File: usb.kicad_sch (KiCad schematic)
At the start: 22 parts, among them Q1 MMBT3904-C20526, Q2 MMBT3904-C20526, SW2 SW_Push, U1 CP2102N-A02-GQFN24R

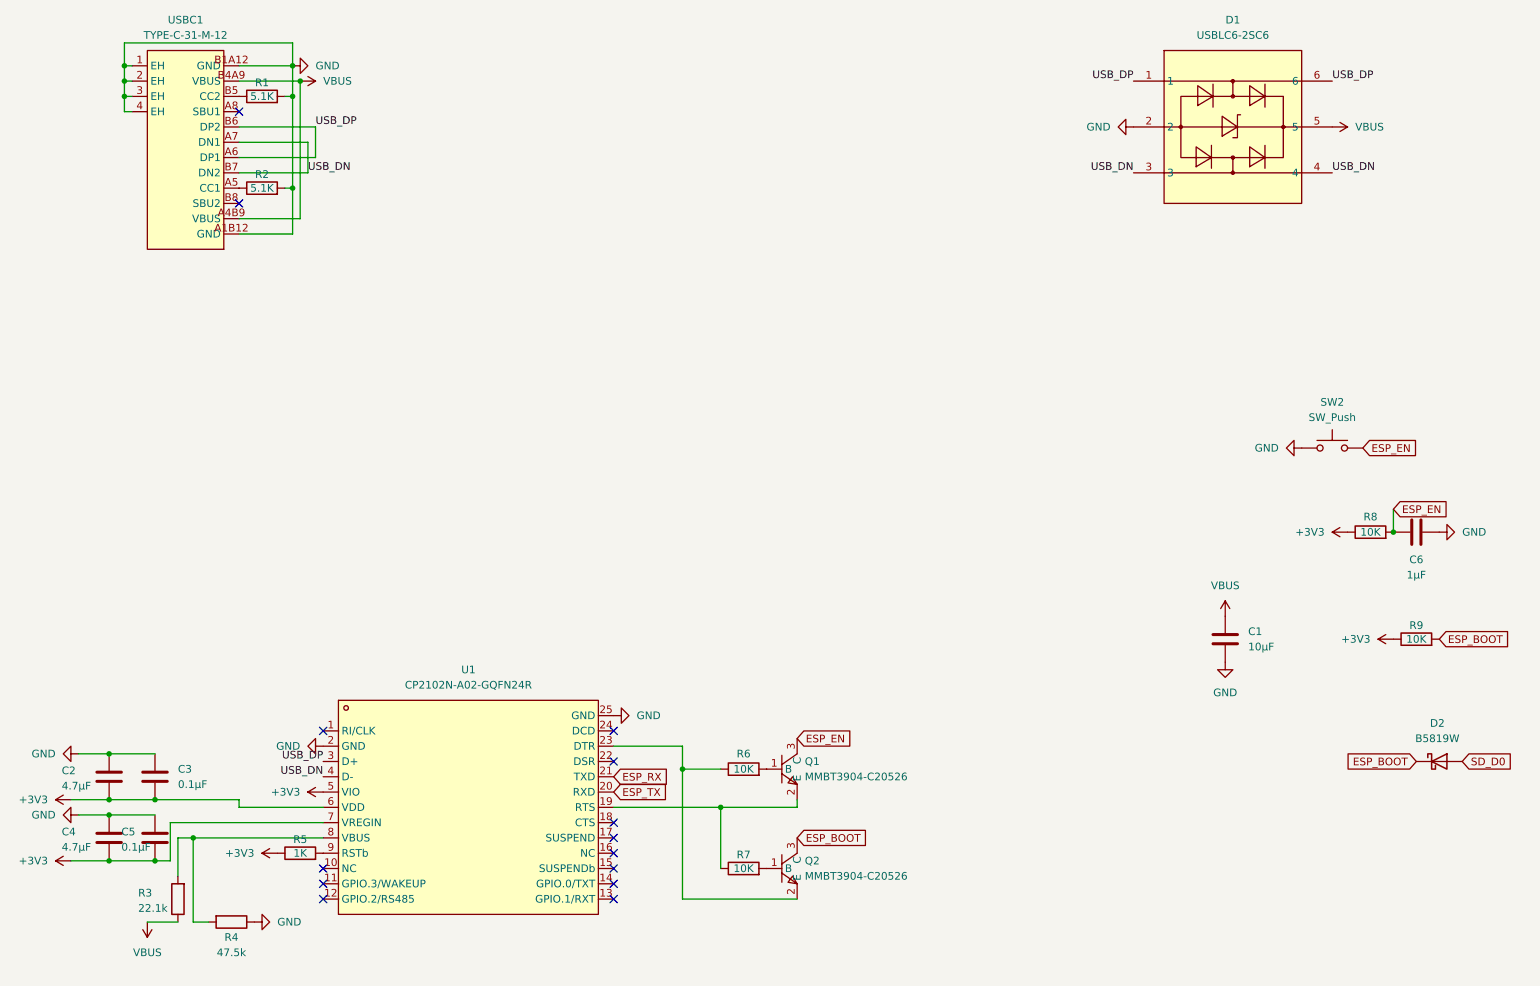
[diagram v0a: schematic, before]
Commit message: Schematic done
- sheet files renamed to English (usb, power, esp32, audio, io)
- final layout, annotation R1-R42 / C1-C43 / U1-U9 / J1-J4 / SW1-SW8
- all buttons are TS-1088, project R/C symbols, PWR_FLAGs
- connections.md replaces conexiuni.md (English, final references)
- final check on the KiCad netlist: 278/278 checks against connections.md
- status updated; firmware note: BQ25180 charge current defaults to ~10 mA

Co-Authored-By: Claude Opus 5.5 <noreply@anthropic.com>
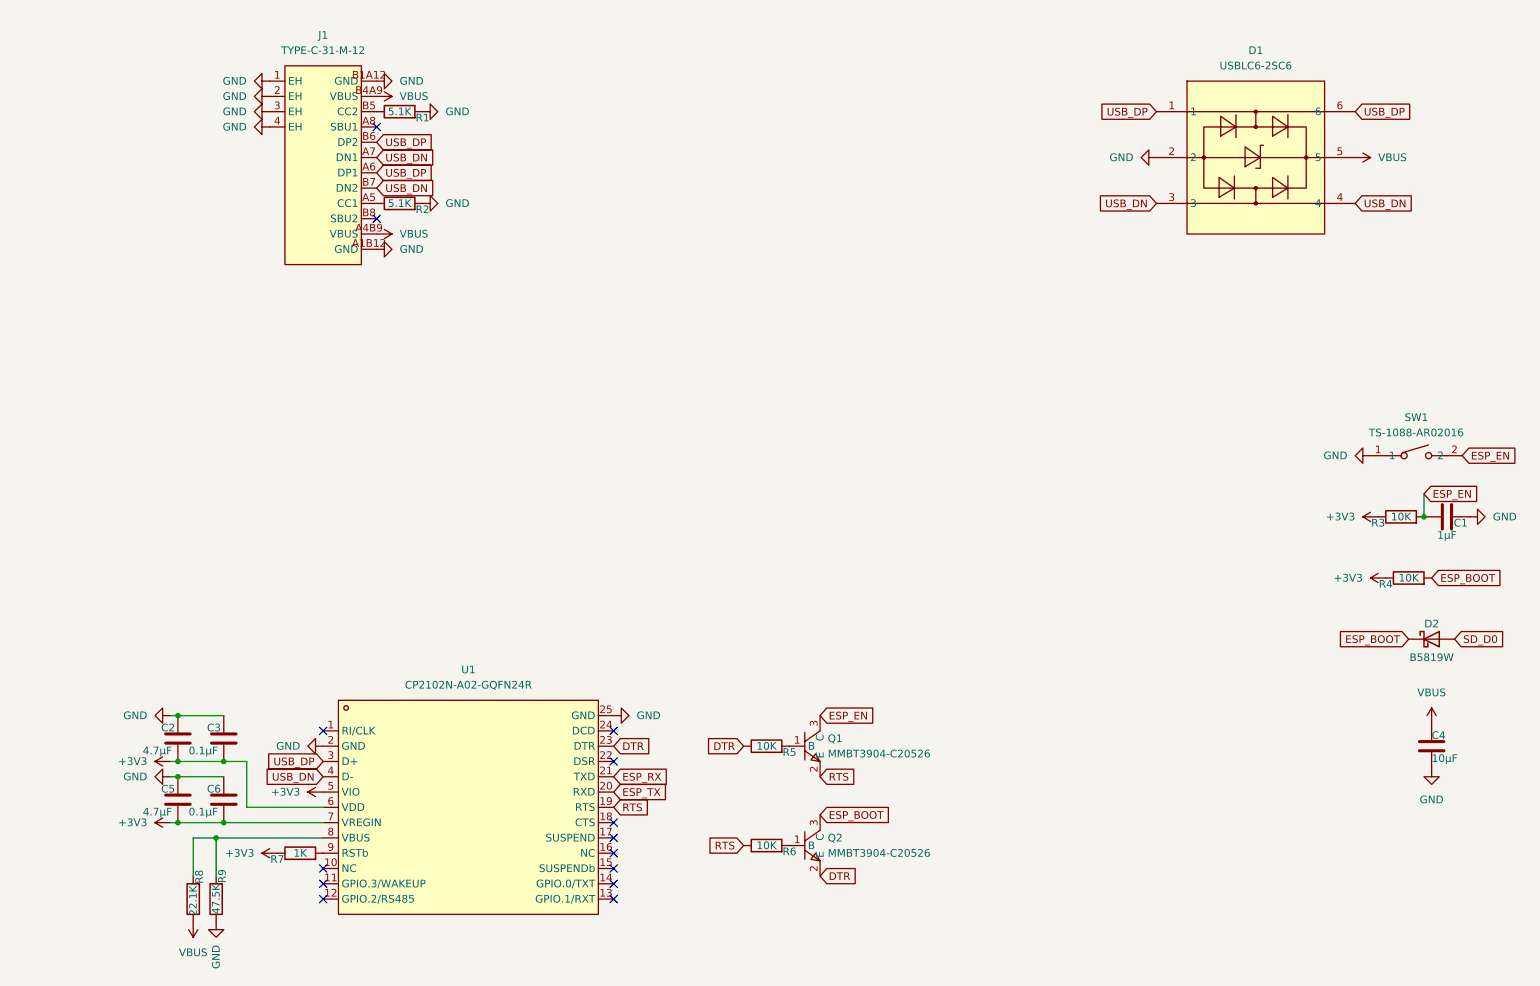
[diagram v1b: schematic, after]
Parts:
- removed SW2: SW_Push, symbol Switch:SW_Push
- added SW1: TS-1088-AR02016, mp3_player:SW-SMD_L3.9-W3.0-P4.45, symbol mp3_player:TS-1088-AR02016
- R1, R2: symbol Device:R -> mp3_player:R
- R3: renamed from R8; symbol Device:R -> mp3_player:R
- R4: renamed from R9; symbol Device:R -> mp3_player:R
- R5: renamed from R6; symbol Device:R -> mp3_player:R
- R6: renamed from R7; symbol Device:R -> mp3_player:R
- R7: renamed from R5; symbol Device:R -> mp3_player:R
- R8: renamed from R3; value 22.1k -> 22.1K; symbol Device:R -> mp3_player:R
- R9: renamed from R4; value 47.5k -> 47.5K; symbol Device:R -> mp3_player:R
- renumbered C6 to C1, C1 to C4, C4 to C5, C5 to C6, USBC1 to J1
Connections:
- net ESP_EN: now also SW1.2
- net GND: now also SW1.1
- net RTS: now reaches Q1.2 (E), R6.1, U1.19 (RTS)
- net DTR: now reaches Q2.2 (E), R5.1, U1.23 (DTR)
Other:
- moved on the sheet: C1, C2, C3, C4, C5, C6, D1, D2, J1, Q1, Q2, R1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

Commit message: Assign footprints and LCSC parts to passives, D2 and BT1
Thin-film 0.1% resistors in the audio path and rail dividers, C0G caps
in the DAC output filter, Samsung/Murata MLCCs with 0603/0805 cases for
bulk caps. Passive choices documented in mp3_player.md.

Co-Authored-By: Claude Opus 5.5 <noreply@anthropic.com>
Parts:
- C1: footprint (none) -> Capacitor_SMD:C_0402_1005Metric; LCSC Part (none) -> C52923
- C2, C5: footprint (none) -> Capacitor_SMD:C_0603_1608Metric; LCSC Part (none) -> C19666
- C3, C6: footprint (none) -> Capacitor_SMD:C_0402_1005Metric; LCSC Part (none) -> C1525
- C4: footprint (none) -> Capacitor_SMD:C_0805_2012Metric; LCSC Part (none) -> C15850
- D2: footprint (none) -> Diode_SMD:D_SOD-123; LCSC Part (none) -> C8598
- R1, R2: footprint (none) -> Resistor_SMD:R_0402_1005Metric; LCSC Part (none) -> C25905
- R3, R4, R5, R6: footprint (none) -> Resistor_SMD:R_0402_1005Metric; LCSC Part (none) -> C190095
- R7: footprint (none) -> Resistor_SMD:R_0402_1005Metric; LCSC Part (none) -> C11702
- R8: footprint (none) -> Resistor_SMD:R_0402_1005Metric; LCSC Part (none) -> C163478
- R9: footprint (none) -> Resistor_SMD:R_0402_1005Metric; LCSC Part (none) -> C137974
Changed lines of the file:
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@@
 			)
 		)
-		(property "Footprint" ""
+		(property "Footprint" "Resistor_SMD:R_0402_1005Metric"
+			(at 48.768 173.99 90)
+			(hide yes)
+			(show_name no)
+			(do_not_autoplace no)
+			(effects
+				(font
+					(size 1.27 1.27)
+				)
+			)
+		)
+				(property "LCSC Part" "C137974"
 			(at 48.768 173.99 90)
 			(hide yes)
@@
 			)
 		)
-		(property "Footprint" ""
+		(property "Footprint" "Resistor_SMD:R_0402_1005Metric"
+			(at 243.84 112.268 90)
+			(hide yes)
+			(show_name no)
+			(do_not_autoplace no)
+			(effects
+				(font
+					(size 1.27 1.27)
+				)
+			)
+		)
+				(property "LCSC Part" "C190095"
 			(at 243.84 112.268 90)
 			(hide yes)
@@
 			)
 		)
-		(property "Footprint" ""
+		(property "Footprint" "Resistor_SMD:R_0402_1005Metric"
+			(at 60.96 168.148 90)
+			(hide yes)
+			(show_name no)
+			(do_not_autoplace no)
+			(effects
+				(font
+					(size 1.27 1.27)
+				)
+			)
+		)
+				(property "LCSC Part" "C11702"
 			(at 60.96 168.148 90)
 			(hide yes)
@@
 			)
 		)
-		(property "Footprint" ""
+		(property "Footprint" "Capacitor_SMD:C_0603_1608Metric"
+			(at 39.6748 143.51 0)
+			(hide yes)
+			(show_name no)
+			(do_not_autoplace no)
+			(effects
+				(font
+					(size 1.27 1.27)
+				)
+			)
+		)
+				(property "LCSC Part" "C19666"
 			(at 39.6748 143.51 0)
 			(hide yes)
@@
 			)
 		)
-		(property "Footprint" ""
+		(property "Footprint" "Resistor_SMD:R_0402_1005Metric"
+			(at 44.958 173.99 90)
+			(hide yes)
+			(show_name no)
+			(do_not_autoplace no)
+			(effects
+				(font
+					(size 1.27 1.27)
+				)
+			)
+		)
+				(property "LCSC Part" "C163478"
 			(at 44.958 173.99 90)
 			(hide yes)
@@
 			)
 		)
-		(property "Footprint" ""
+		(property "Footprint" "Resistor_SMD:R_0402_1005Metric"
+			(at 245.11 122.428 90)
+			(hide yes)
+			(show_name no)
+			(do_not_autoplace no)
+			(effects
+				(font
+					(size 1.27 1.27)
+				)
+			)
+		)
+				(property "LCSC Part" "C190095"
 			(at 245.11 122.428 90)
 			(hide yes)
@@
 			)
 		)
-		(property "Footprint" ""
+		(property "Footprint" "Resistor_SMD:R_0402_1005Metric"
+			(at 138.43 166.878 90)
+			(hide yes)
+			(show_name no)
+			(do_not_autoplace no)
+			(effects
+				(font
+					(size 1.27 1.27)
+				)
+			)
+		)
+				(property "LCSC Part" "C190095"
 			(at 138.43 166.878 90)
 			(hide yes)
@@
 			)
 		)
-		(property "Footprint" ""
+		(property "Footprint" "Resistor_SMD:R_0402_1005Metric"
+			(at 138.43 150.368 90)
+			(hide yes)
+			(show_name no)
+			(do_not_autoplace no)
+			(effects
+				(font
+					(size 1.27 1.27)
+				)
+			)
+		)
+				(property "LCSC Part" "C190095"
 			(at 138.43 150.368 90)
 			(hide yes)
@@
 			)
 		)
-		(property "Footprint" ""
+		(property "Footprint" "Capacitor_SMD:C_0603_1608Metric"
+			(at 39.6748 153.67 0)
+			(hide yes)
+			(show_name no)
+			(do_not_autoplace no)
+			(effects
+				(font
+					(size 1.27 1.27)
+				)
+			)
+		)
+				(property "LCSC Part" "C19666"
 			(at 39.6748 153.67 0)
 			(hide yes)
@@
 			)
 		)
-		(property "Footprint" ""
+		(property "Footprint" "Capacitor_SMD:C_0402_1005Metric"
+			(at 47.2948 153.67 0)
+			(hide yes)
+			(show_name no)
+			(do_not_autoplace no)
+			(effects
+				(font
+					(size 1.27 1.27)
+				)
+			)
+		)
+				(property "LCSC Part" "C1525"
 			(at 47.2948 153.67 0)
 			(hide yes)
@@
 			)
 		)
-		(property "Footprint" ""
+		(property "Footprint" "Capacitor_SMD:C_0805_2012Metric"
+			(at 249.8852 152.4 0)
+			(hide yes)
+			(show_name no)
+			(do_not_autoplace no)
+			(effects
+				(font
+					(size 1.27 1.27)
+				)
+			)
+		)
+				(property "LCSC Part" "C15850"
 			(at 249.8852 152.4 0)
 			(hide yes)
@@
 			)
 		)
-		(property "Footprint" ""
+		(property "Footprint" "Capacitor_SMD:C_0402_1005Metric"
+			(at 247.65 111.4552 0)
+			(hide yes)
+			(show_name no)
+			(do_not_autoplace no)
+			(effects
+				(font
+					(size 1.27 1.27)
+				)
+			)
+		)
+				(property "LCSC Part" "C52923"
 			(at 247.65 111.4552 0)
 			(hide yes)
@@
 			)
 		)
-		(property "Footprint" ""
+		(property "Footprint" "Capacitor_SMD:C_0402_1005Metric"
+			(at 47.2948 143.51 0)
+			(hide yes)
+			(show_name no)
+			(do_not_autoplace no)
+			(effects
+				(font
+					(size 1.27 1.27)
+				)
+			)
+		)
+				(property "LCSC Part" "C1525"
 			(at 47.2948 143.51 0)
 			(hide yes)
@@
 			)
 		)
-		(property "Footprint" ""
+		(property "Footprint" "Resistor_SMD:R_0402_1005Metric"
+			(at 77.47 60.198 90)
+			(hide yes)
+			(show_name no)
+			(do_not_autoplace no)
+			(effects
+				(font
+					(size 1.27 1.27)
+				)
+			)
+		)
+				(property "LCSC Part" "C25905"
 			(at 77.47 60.198 90)
 			(hide yes)
@@
 			)
 		)
-		(property "Footprint" ""
+		(property "Footprint" "Diode_SMD:D_SOD-123"
+			(at 248.92 130.81 0)
+			(hide yes)
+			(show_name no)
+			(do_not_autoplace no)
+			(effects
+				(font
+					(size 1.27 1.27)
+				)
+			)
+		)
+				(property "LCSC Part" "C8598"
 			(at 248.92 130.81 0)
 			(hide yes)
@@
 			)
 		)
-		(property "Footprint" ""
+		(property "Footprint" "Resistor_SMD:R_0402_1005Metric"
+			(at 77.47 44.958 90)
+			(hide yes)
+			(show_name no)
+			(do_not_autoplace no)
+			(effects
+				(font
+					(size 1.27 1.27)
+				)
+			)
+		)
+				(property "LCSC Part" "C25905"
 			(at 77.47 44.958 90)
 			(hide yes)

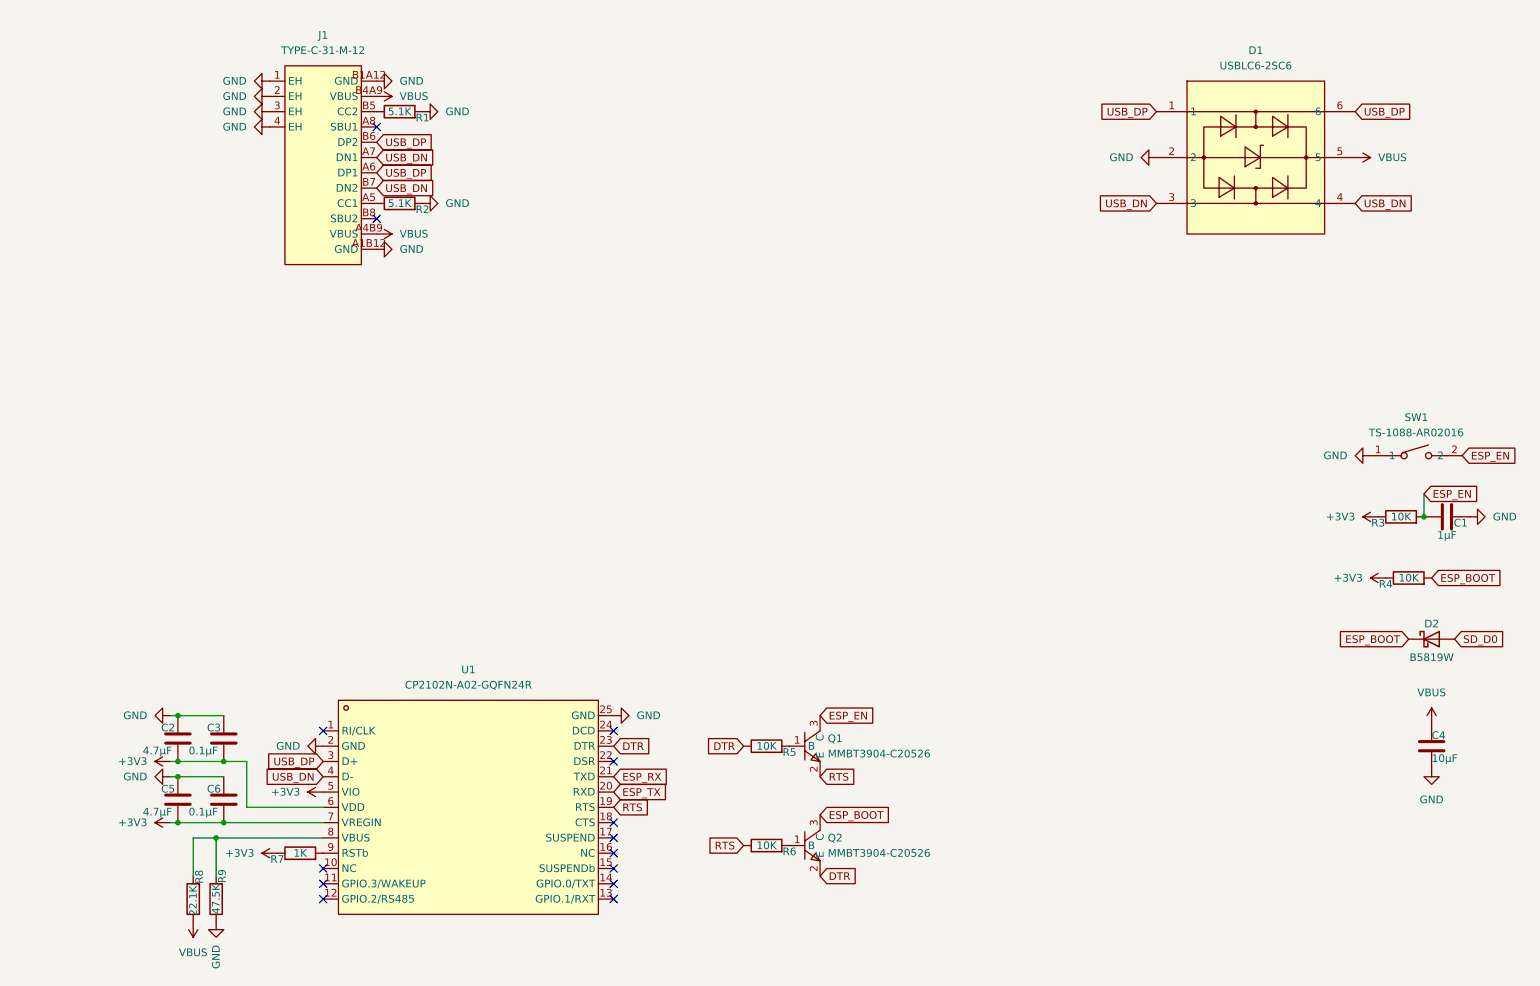
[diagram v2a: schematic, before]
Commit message: Fix ERC and document enclosure concept
- ERC clean: power flags moved onto real nets, USBLC6 pin types,
  Unspecified pins allowed in the pin conflict map, off-grid wires aligned
- mp3_player.md: enclosure section (anodized aluminium v1, titanium v2,
  printed click wheel and antenna cap, build123d workflow)
- ignore the build123d venv

Co-Authored-By: Claude Opus 5.5 <noreply@anthropic.com>
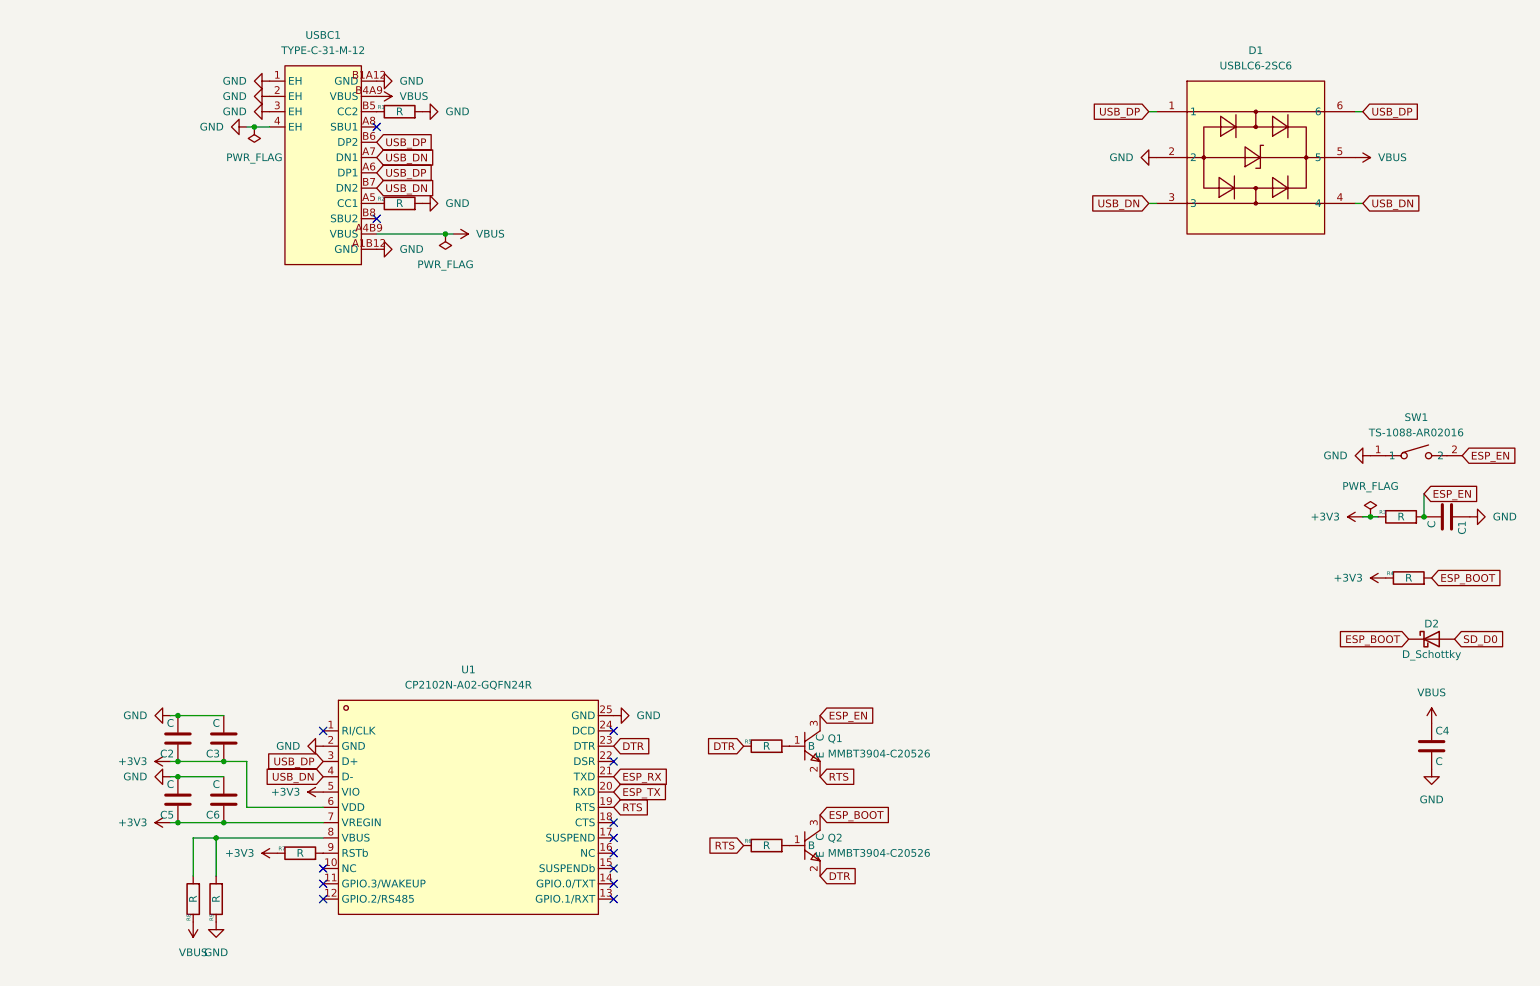
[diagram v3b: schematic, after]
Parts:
- C1: value 1µF -> C
- C2, C5: value 4.7µF -> C
- C3, C6: value 0.1µF -> C
- C4: value 10µF -> C
- D2: value B5819W -> D_Schottky
- R1, R2: value 5.1K -> R
- R3, R4, R5, R6: value 10K -> R
- R7: value 1K -> R
- R8: value 22.1K -> R
- R9: value 47.5K -> R
- renumbered J1 to USBC1
